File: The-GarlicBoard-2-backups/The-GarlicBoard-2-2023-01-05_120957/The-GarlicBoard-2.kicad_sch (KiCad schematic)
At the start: 314 parts, among them J1 TYPE-C-31-M12_13, J2 PAD_SQUARE_1MM, J3 PAD_SQUARE_1MM, J4 PAD_SQUARE_1MM, J5 PAD_SQUARE_1MM, J6 Conn_01x04, K1 SMD-SWITCH-TACTILE-SPST-NO_4P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, Q1 MUN5311DW1T1G, Q2 MUN5311DW1T1G, SW1 RotaryEncoder_Switch, SW10 W, SW11 S, SW12 X, SW13 L_CMD, SW14 E, SW15 D, SW16 C, SW17 R, SW18 F, SW19 V, SW2 ESC, SW20 FN_1, SW21 T, SW22 G, SW23 B, SW24 Y, SW25 H, SW26 N, SW27 SPACE, SW28 U, SW29 J, SW3 TAB, SW30 M, SW31 I, SW32 K, SW33 COMMA, SW34 R_CMD, SW35 O, SW36 L, SW37 PERIOD, SW38 P, SW39 SEMI_COLON, SW4 L_SHIFT, SW40 SLASH, SW41 R_ALT, SW42 HYPHEN, SW43 APOSTROPHE, SW44 R_SHIFT, SW45 R_CTRL, SW46 EQUALS, SW47 RETURN, SW48 FN_2, SW49 BCK_SPC, SW5 L_CTRL, SW50 7, SW51 4, SW52 1, SW53 0, SW54 8, SW55 5, SW56 2, SW57 00, SW58 9, SW59 6, SW6 Q, SW60 3, SW61 NUM_PER, SW62 MINUS, SW63 PLUS, SW64 ENTER, SW65 PAD_LOCK, SW7 A, SW8 Z, SW9 L_ALT, U1 STM32F411CEU6, U2 SRV05-4, U3 SN74LV1T34DCKR, U4 AAP2967-33VIR1, U5 MB85RS64PNF-G-JNERE1, U6 SN74LV1T34DCKR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

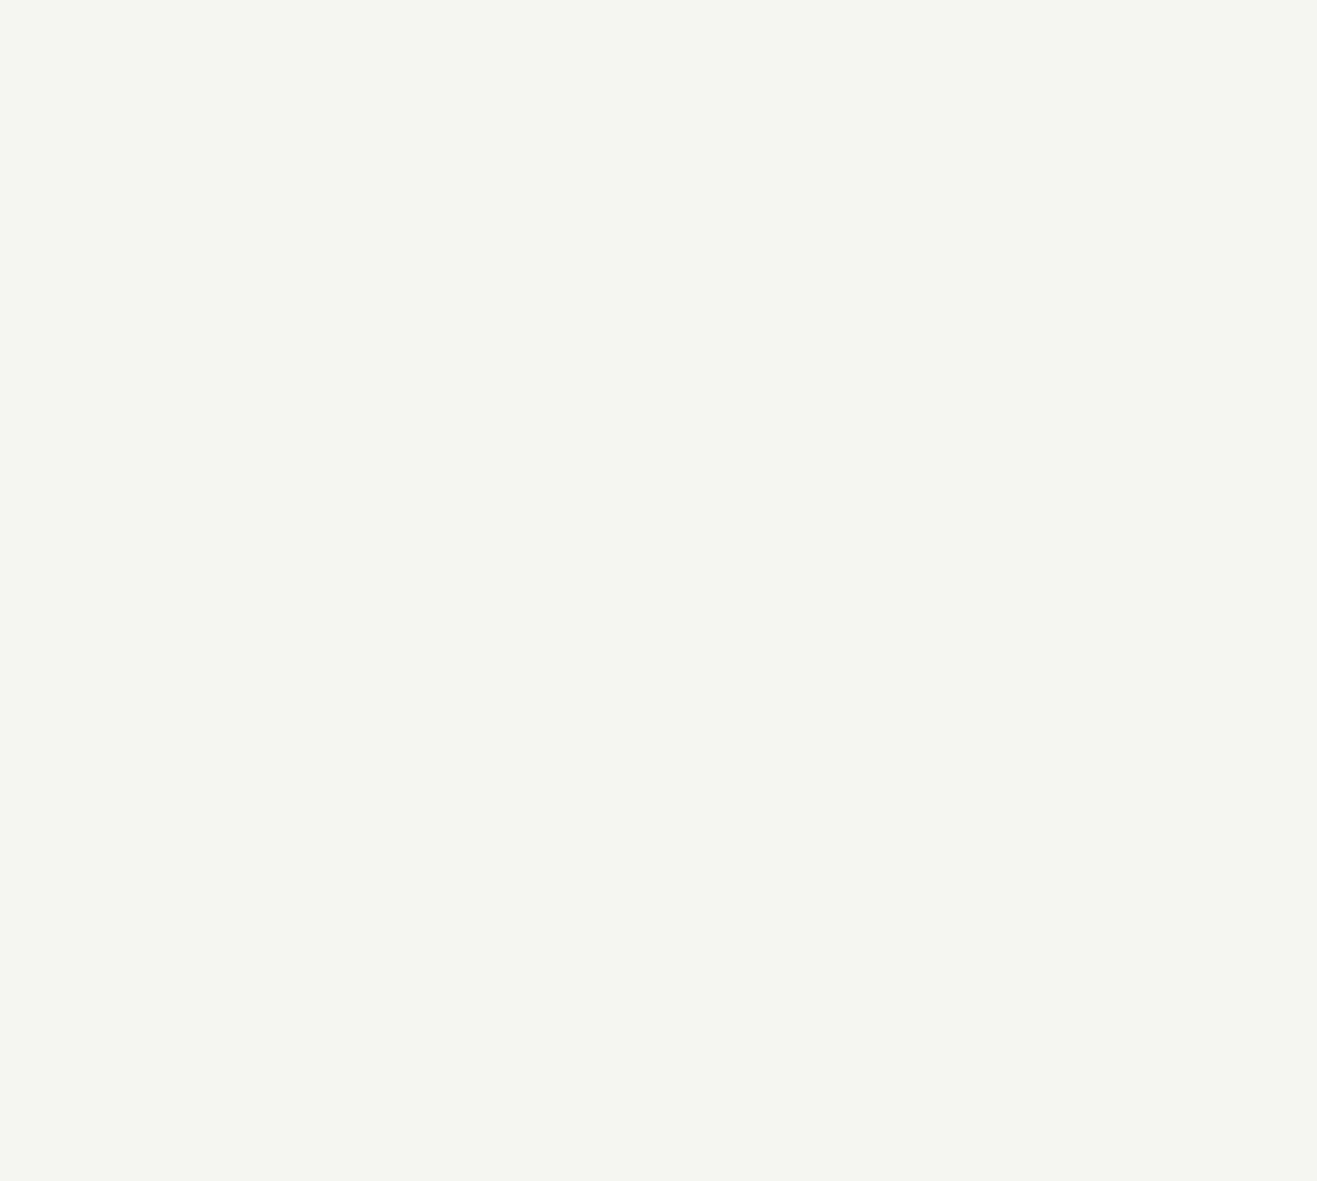
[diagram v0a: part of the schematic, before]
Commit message: Rotated clock, trimmed edge cuts
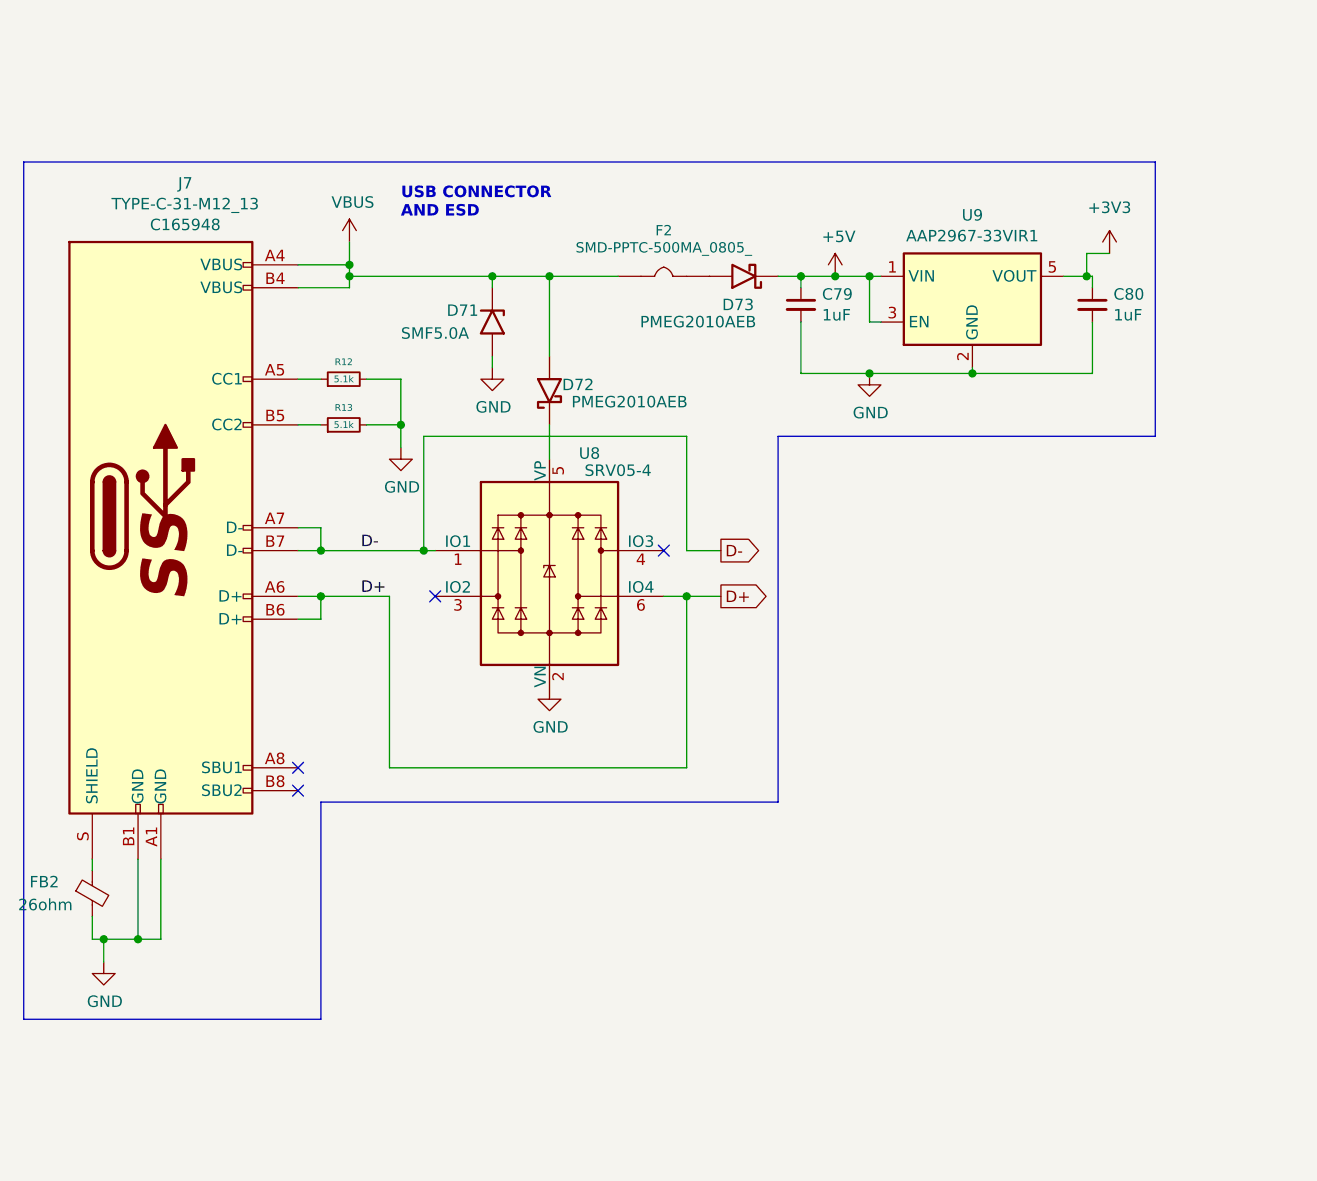
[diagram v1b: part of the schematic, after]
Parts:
- added C79, C80: cap_1uF_10v_0402, Bonsai_C4:C_0402_1005Metric, symbol Bonsai_C4:cap_1uF_10v_0402
- added D71: SMF5.0A, Bonsai_C4:D_SOD-123FL, symbol Bonsai_C4:SMF5.0A
- added D72, D73: PMEG2010AEB, Diode_SMD:D_SOD-523, symbol Bonsai_C4:PMEG2010AEB
- added F2: SMD-PPTC-500MA_0805_, Bonsai_C4:F0805, symbol Bonsai_C4:SMD-PPTC-500MA_0805_
- added FB2: fb_0402_26ohm, Bonsai_C4:R_0402_1005Metric, symbol Bonsai_C4:fb_0402_26ohm
- added J7: TYPE-C-31-M12_13, Bonsai_C4:TYPE-C-31-M-12, symbol Bonsai_C4:TYPE-C-31-M12_13
- added R12, R13: 5.1k, Keebio-Parts:R_0402, symbol Device:R_Small
- added U8: SRV05-4, marbastlib-various:SOT-23-6-routable, symbol Bonsai_C4:SRV05-4
- added U9: AAP2967-33VIR1, Bonsai_C4:SOT-23-5, symbol Bonsai_C4:AAP2967-33VIR1
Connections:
- net +3V3: now also C80.1, U9.5 (VOUT)
- net +5V: now also C79.1, D73.1 (K), U9.1 (VIN), U9.3 (EN)
- net D+: now also J7.A6 (D+), J7.B6 (D+), U8.6 (IO4)
- net D-: now also J7.A7 (D-), J7.B7 (D-), U8.1 (IO1)
- net GND: now also C79.2, C80.2, D71.2 (A2), FB2.2, J7.A1 (GND), J7.B1 (GND), R12.2, R13.2, U8.2 (VN), U9.2 (GND)
- net VBUS: now also D71.1 (A1), D72.2 (A), F2.2, J7.A4 (VBUS), J7.B4 (VBUS)
- new net: D73.2 (A), F2.1
- new net: D72.1 (K), U8.5 (VP)
- new net: FB2.1, J7.S (SHIELD)
- new net: J7.A5 (CC1), R12.1
- new net: J7.B5 (CC2), R13.1
- no-connect marks 11 -> 15
